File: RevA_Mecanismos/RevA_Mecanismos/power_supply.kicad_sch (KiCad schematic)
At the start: 4 parts

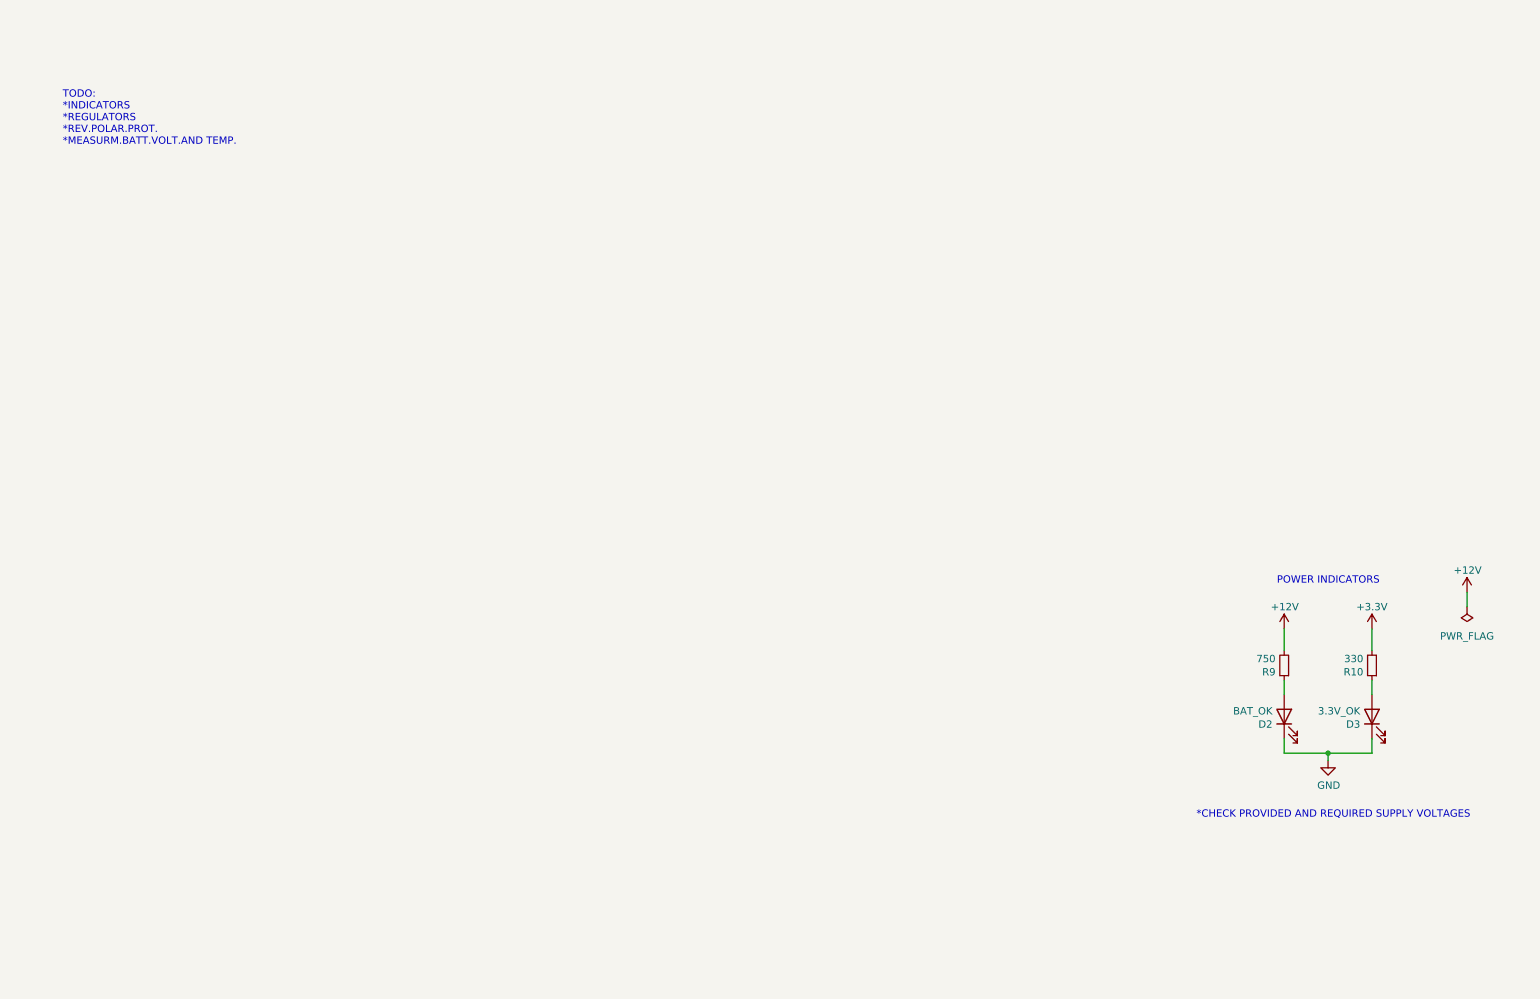
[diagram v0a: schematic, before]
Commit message: Added H-Bridges and voltage regulators
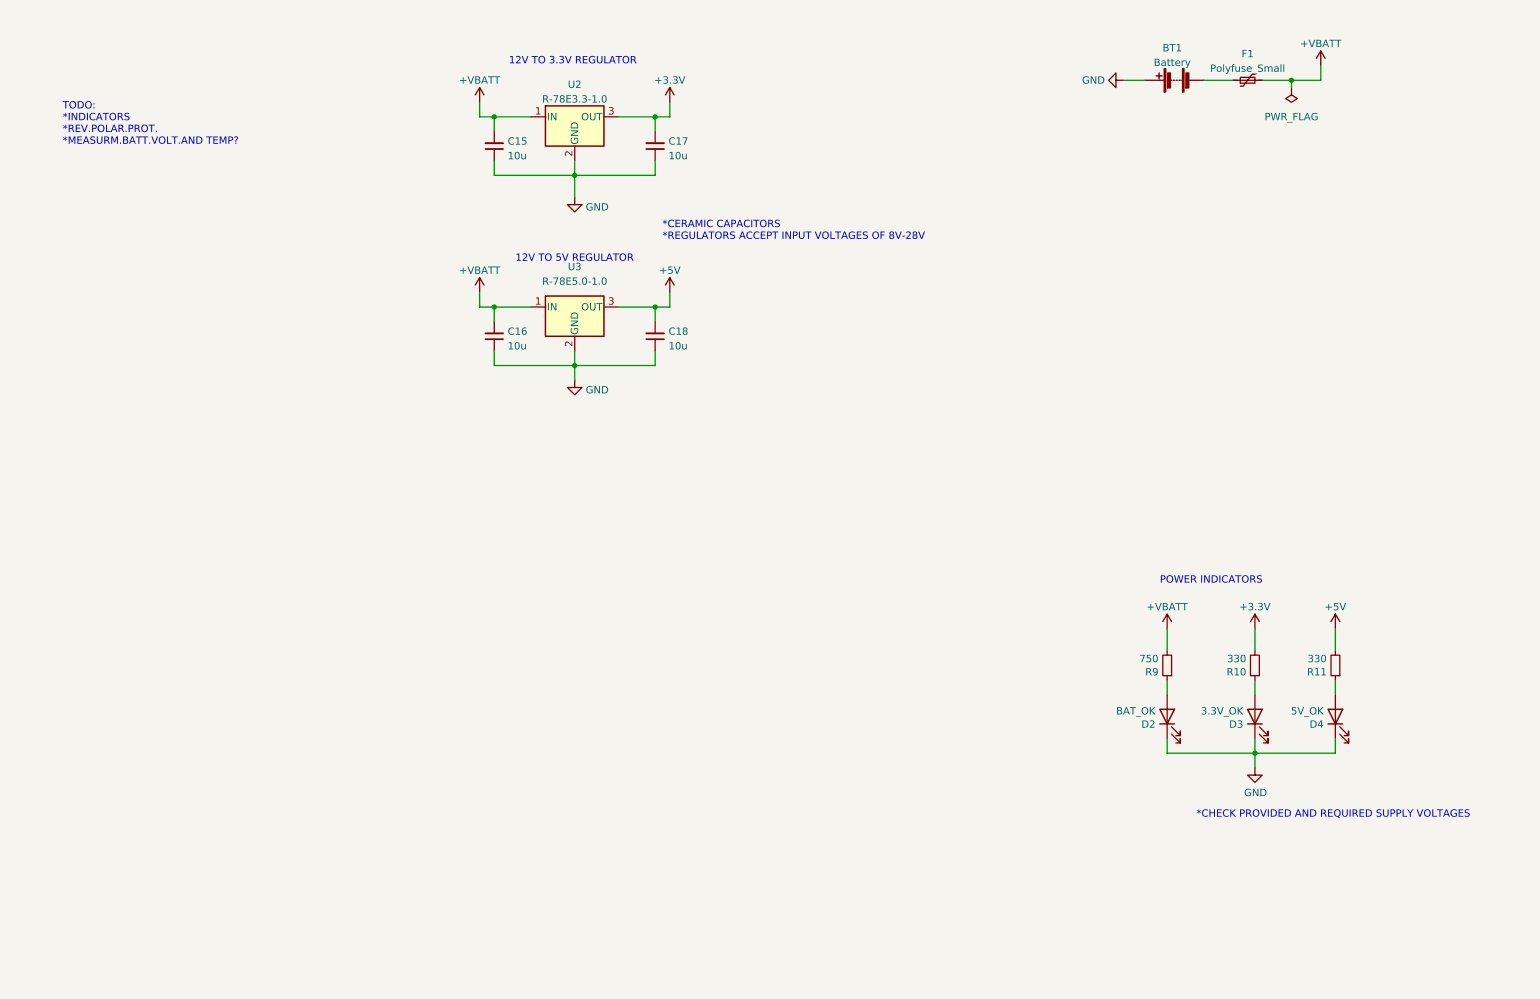
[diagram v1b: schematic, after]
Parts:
- added BT1: Battery, Connector_AMASS:AMASS_XT60-M_1x02_P7.20mm_Vertical, symbol Device:Battery
- added C15, C16, C17, C18: 10u, Capacitor_SMD:C_0603_1608Metric, symbol Device:C_Small
- added D4: 5V_OK, LED_SMD:LED_0603_1608Metric, symbol Device:LED
- added F1: Polyfuse_Small, Fuse:Fuse_2920_7451Metric, symbol Device:Polyfuse_Small
- added R11: 330, Resistor_SMD:R_0603_1608Metric, symbol Device:R_Small
- added U2: R-78E3.3-1.0, Converter_DCDC:Converter_DCDC_RECOM_R-78E-0.5_THT, symbol Regulator_Switching:R-78E3.3-1.0
- added U3: R-78E5.0-1.0, Converter_DCDC:Converter_DCDC_RECOM_R-78E-0.5_THT, symbol Regulator_Switching:R-78E5.0-1.0
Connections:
- net +3.3V: now also C17.2, U2.3 (OUT)
- net GND: now also BT1.1 (+), C15.1, C16.1, C17.1, C18.1, D4.1 (K), U2.2 (GND), U3.2 (GND)
- net +12V renamed +VMOT
- net +VMOT: now also C15.2, C16.2, F1.2, U2.1 (IN), U3.1 (IN)
- new net: D4.2 (A), R11.1
- new net: BT1.2 (-), F1.1
- new net +5V: C18.2, R11.2, U3.3 (OUT)
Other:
- note added: "*CERAMIC CAPACITORS *REGULATORS ACCEPT INPUT VOLTAGES OF 8V-28V"
- note added: "12V TO 3.3V REGULATOR"
- note added: "12V TO 5V REGULATOR"
- note added: "TODO: *INDICATORS *REV.POLAR.PROT. *MEASURM.BATT.VOLT.AND TEMP?"
- note removed: "TODO: *INDICATORS *REGULATORS *REV.POLAR.PROT. *MEASURM.BATT.VOLT.AND TEMP."
- moved on the sheet: D2, D3, R10, R9

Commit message: Created PCB project
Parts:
- removed BT1: Battery, Connector_AMASS:AMASS_XT60-M_1x02_P7.20mm_Vertical, symbol Device:Battery
- added BT1: Battery, Connector_AMASS:AMASS_XT60-M_1x02_P7.20mm_Vertical, symbol CustomUtilities:Battery
- added Q1: NDS352AP, NDS352AP:SOT95P237X111-3N, symbol NDS352AP:NDS352AP
- added R20: 100k, Resistor_SMD:R_0603_1608Metric, symbol Device:R_Small
- added Z1: MMSZ4702T1G, MMSZ4702T1G:SOD3716X135N, symbol MMSZ4702T1G:MMSZ4702T1G
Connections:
- net +VMOT: now also Q1.2, Z1.1; no longer F1.2
- net GND: now also BT1.1 (-), R20.1
- net at F1.1: now also BT1.2 (+)
- new net: Q1.1, R20.2, Z1.2
- new net BATT_CONN: F1.2, Q1.3
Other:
- note added: "3.3V REGULATOR"
- note added: "5V REGULATOR"
- note added: "Power"
- note added: "REVERSE POLARITY PROT."
- note added: "TODO: *MEASURM.BATT.VOLT.AND TEMP?"
- note removed: "*CHECK PROVIDED AND REQUIRED SUPPLY VOLTAGES"
- note removed: "12V TO 3.3V REGULATOR"
- note removed: "12V TO 5V REGULATOR"
- note removed: "TODO: *INDICATORS *REV.POLAR.PROT. *MEASURM.BATT.VOLT.AND TEMP?"
- moved on the sheet: C15, C16, C17, C18, F1, U2, U3

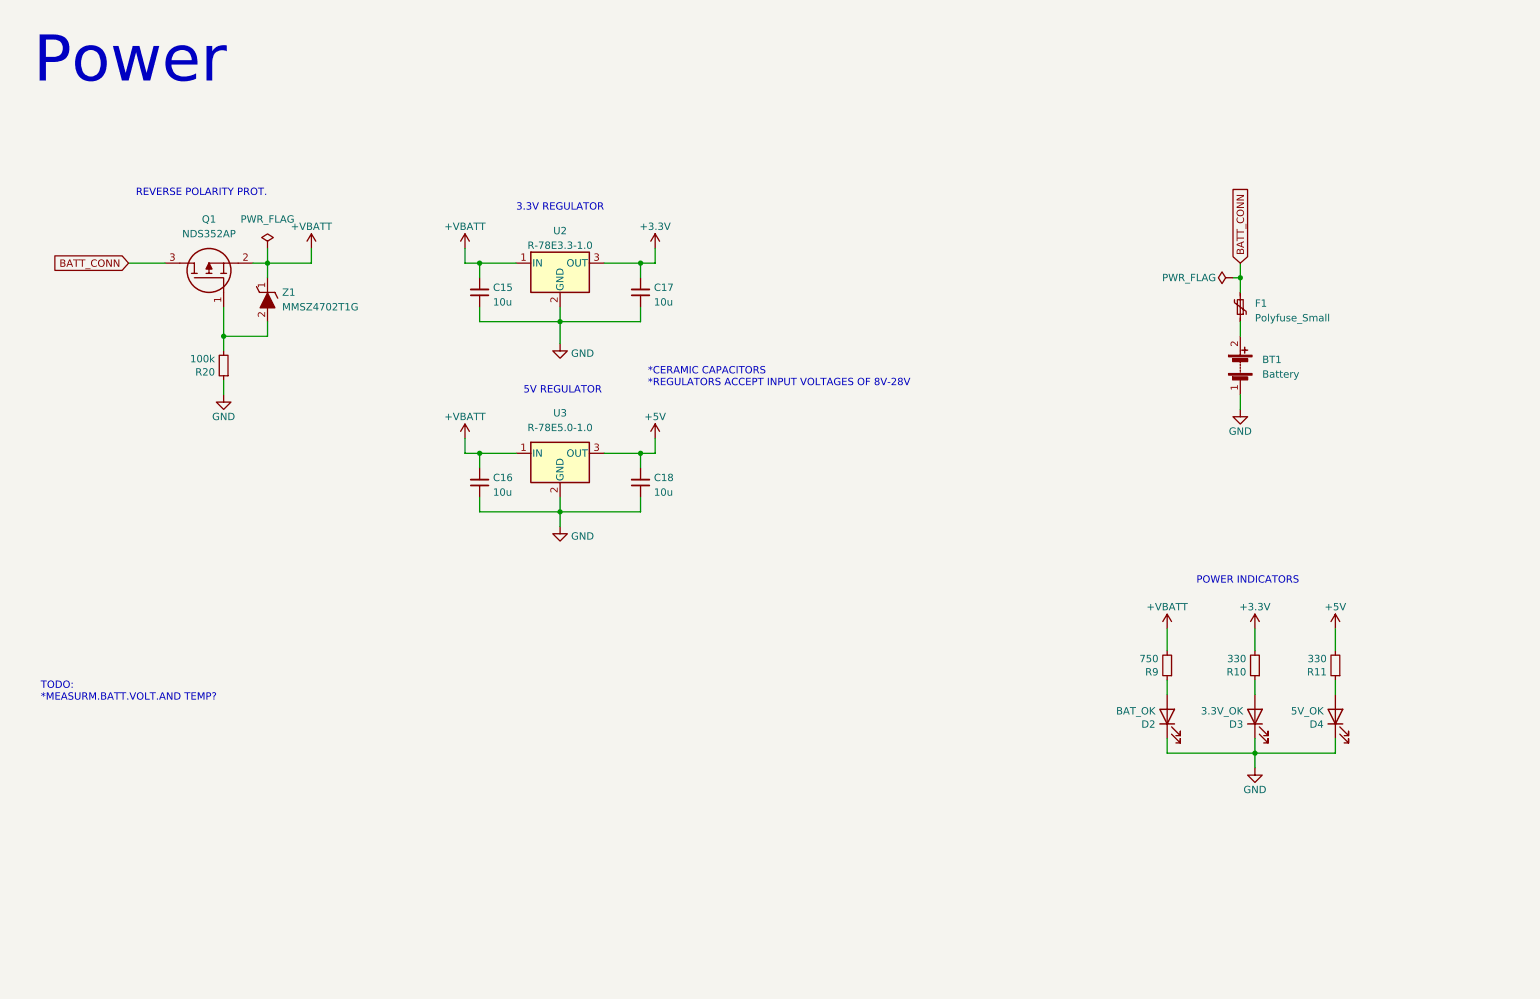
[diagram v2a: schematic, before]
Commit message: Adiciones a secciones de motores y power supply para placa de mecanismos
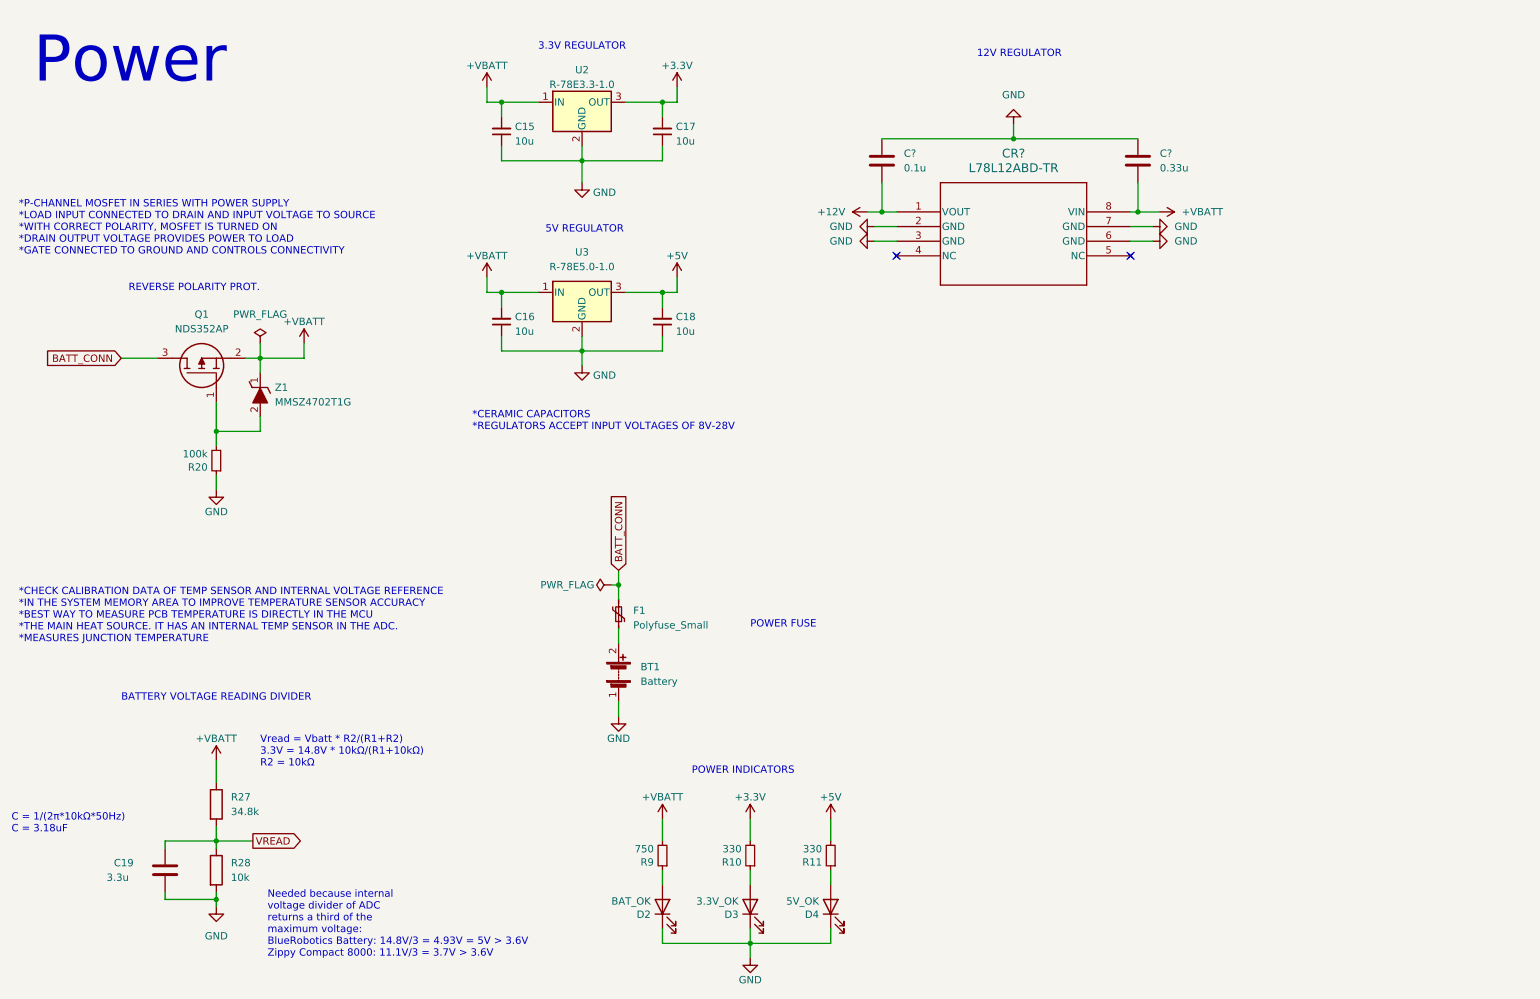
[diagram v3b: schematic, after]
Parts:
- added C19: 3.3u, symbol Device:C
- added C?: 0.33u, symbol Device:C
- added C?: 0.1u, symbol Device:C
- added CR?: L78L12ABD-TR, SO-8_STM, symbol L78L12ABD-TR:L78L12ABD-TR
- added R27: 34.8k, symbol Device:R
- added R28: 10k, symbol Device:R
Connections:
- net +VMOT: now also C?.2, CR?.8 (VIN), R27.1
- net GND: now also C19.2, C?.1, C?.1, CR?.2 (GND), CR?.3 (GND), CR?.6 (GND), CR?.7 (GND), R28.2
- new net +12V: C?.2, CR?.1 (VOUT)
- new net VREAD: C19.1, R27.2, R28.1
- no-connect marks 0 -> 2
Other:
- note added: "*CHECK CALIBRATION DATA OF TEMP SENSOR AND INTERNAL VOLTAGE REFERENCE *IN THE SYSTEM MEMORY AREA TO IMPROVE TEMPERATURE SENSOR ACCURACY *BEST WAY TO MEASURE PCB TEMPERATURE IS DIRECTLY IN THE MCU *THE MAIN HEAT SOURCE. IT HAS AN INTERNAL TEMP SENSOR IN THE ADC. *MEASURES JUNCTION TEMPERATURE"
- note added: "*P-CHANNEL MOSFET IN SERIES WITH POWER SUPPLY *LOAD INPUT CONNECTED TO DRAIN AND INPUT VOLTAGE TO SOURCE *WITH CORRECT POLARITY, MOSFET IS TURNED ON *DRAIN OUTPUT VOLTAGE PROVIDES POWER TO LOAD *GATE CONNECTED TO GROUND AND CONTROLS CONNECTIVITY"
- note added: "12V REGULATOR"
- note added: "BATTERY VOLTAGE READING DIVIDER"
- note added: "C = 1/(2π*10kΩ*50Hz) C = 3.18uF"
- note added: "Needed because internal voltage divider of ADC returns a third of the maximum voltage: BlueRobotics Battery: 14.8V/3 = 4.93V = 5V > 3.6V Zippy Compact 8000: 11.1V/3 = 3.7V > 3.6V"
- note added: "POWER FUSE"
- note added: "Vread = Vbatt * R2/(R1+R2) 3.3V = 14.8V * 10kΩ/(R1+10kΩ) R2 = 10kΩ"
- note removed: "TODO: *MEASURM.BATT.VOLT.AND TEMP?"
- moved on the sheet: BT1, C15, C16, C17, C18, D2, D3, D4, F1, Q1, R10, R11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
